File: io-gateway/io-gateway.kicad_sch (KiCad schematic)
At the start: 8 parts, among them J1 1752201, J2 1752201, J3 1752201, J4 Screw_Terminal_01x09, J5 Screw_Terminal_01x09, J6 Screw_Terminal_01x09

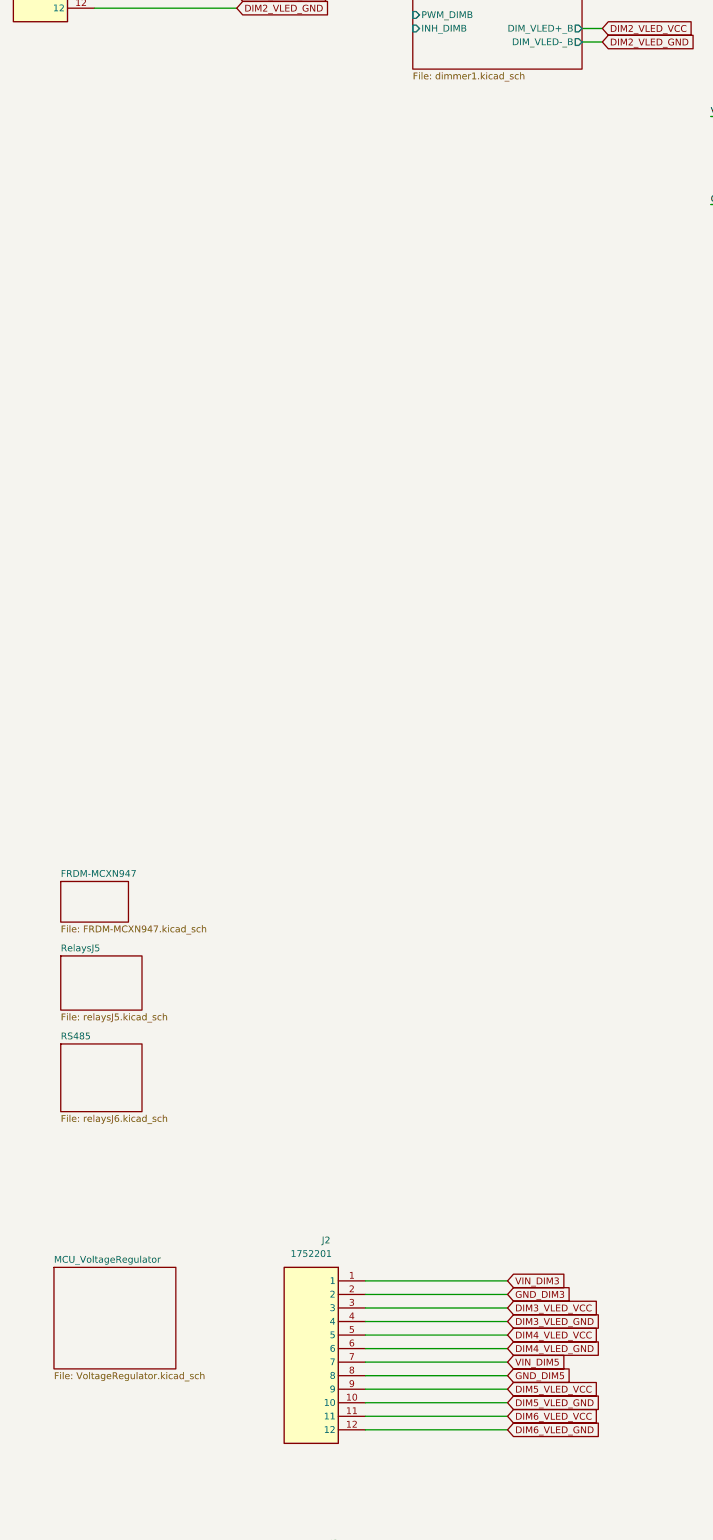
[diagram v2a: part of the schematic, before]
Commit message: reannotate dimmers and relays
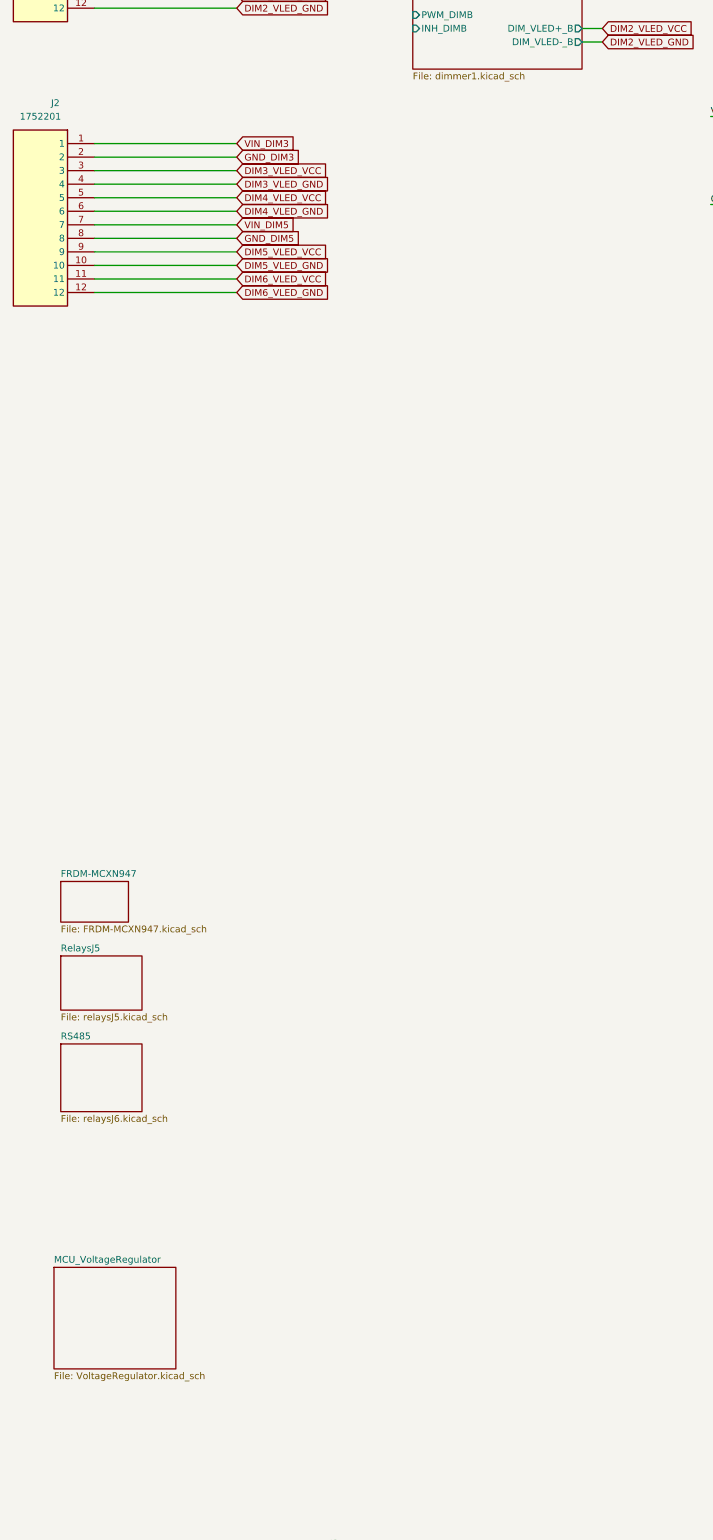
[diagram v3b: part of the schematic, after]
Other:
- moved on the sheet: J2
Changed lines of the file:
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@@
 	(wire
 		(pts
-			(xy 87.63 302.26) (xy 114.3 302.26)
+			(xy 36.83 88.9) (xy 63.5 88.9)
 		)
 		(stroke
@@
 	(wire
 		(pts
-			(xy 87.63 294.64) (xy 114.3 294.64)
+			(xy 36.83 81.28) (xy 63.5 81.28)
 		)
 		(stroke
@@
 	(wire
 		(pts
-			(xy 87.63 322.58) (xy 114.3 322.58)
+			(xy 36.83 109.22) (xy 63.5 109.22)
 		)
 		(stroke
@@
 	(wire
 		(pts
-			(xy 87.63 297.18) (xy 114.3 297.18)
+			(xy 36.83 83.82) (xy 63.5 83.82)
 		)
 		(stroke
@@
 	(wire
 		(pts
-			(xy 87.63 307.34) (xy 114.3 307.34)
+			(xy 36.83 93.98) (xy 63.5 93.98)
 		)
 		(stroke
@@
 	(wire
 		(pts
-			(xy 87.63 312.42) (xy 114.3 312.42)
+			(xy 36.83 99.06) (xy 63.5 99.06)
 		)
 		(stroke
@@
 	(wire
 		(pts
-			(xy 87.63 304.8) (xy 114.3 304.8)
+			(xy 36.83 91.44) (xy 63.5 91.44)
 		)
 		(stroke
@@
 	(wire
 		(pts
-			(xy 87.63 317.5) (xy 114.3 317.5)
+			(xy 36.83 104.14) (xy 63.5 104.14)
 		)
 		(stroke
@@
 	(wire
 		(pts
-			(xy 87.63 299.72) (xy 114.3 299.72)
+			(xy 36.83 86.36) (xy 63.5 86.36)
 		)
 		(stroke
@@
 	(wire
 		(pts
-			(xy 87.63 309.88) (xy 114.3 309.88)
+			(xy 36.83 96.52) (xy 63.5 96.52)
 		)
 		(stroke
@@
 	(wire
 		(pts
-			(xy 87.63 314.96) (xy 114.3 314.96)
-		)
-		(stroke
-			(width 0)
-			(type default)
-		)
-	)
-	(wire
-		(pts
-			(xy 87.63 320.04) (xy 114.3 320.04)
+			(xy 36.83 101.6) (xy 63.5 101.6)
+		)
+		(stroke
+			(width 0)
+			(type default)
+		)
+	)
+	(wire
+		(pts
+			(xy 36.83 106.68) (xy 63.5 106.68)
 		)
 		(stroke
@@
 	(global_label "DIM3_VLED_VCC"
 		(shape input)
-		(at 114.3 299.72 0)
-		(fields_autoplaced yes)
-		(effects
-			(font
-				(size 1.27 1.27)
-			)
-			(justify left)
-		)
-		(property "Intersheetrefs" "${INTERSHEET_REFS}"
-			(at 128.8966 299.72 0)
+		(at 63.5 86.36 0)
+		(fields_autoplaced yes)
+		(effects
+			(font
+				(size 1.27 1.27)
+			)
+			(justify left)
+		)
+		(property "Intersheetrefs" "${INTERSHEET_REFS}"
+			(at 78.0966 86.36 0)
 			(effects
 				(font
@@
 	(global_label "DIM5_VLED_VCC"
 		(shape input)
-		(at 114.3 314.96 0)
-		(fields_autoplaced yes)
-		(effects
-			(font
-				(size 1.27 1.27)
-			)
-			(justify left)
-		)
-		(property "Intersheetrefs" "${INTERSHEET_REFS}"
-			(at 128.8966 314.96 0)
+		(at 63.5 101.6 0)
+		(fields_autoplaced yes)
+		(effects
+			(font
+				(size 1.27 1.27)
+			)
+			(justify left)
+		)
+		(property "Intersheetrefs" "${INTERSHEET_REFS}"
+			(at 78.0966 101.6 0)
 			(effects
 				(font
@@
 	(global_label "DIM6_VLED_VCC"
 		(shape input)
-		(at 114.3 320.04 0)
-		(fields_autoplaced yes)
-		(effects
-			(font
-				(size 1.27 1.27)
-			)
-			(justify left)
-		)
-		(property "Intersheetrefs" "${INTERSHEET_REFS}"
-			(at 128.8966 320.04 0)
+		(at 63.5 106.68 0)
+		(fields_autoplaced yes)
+		(effects
+			(font
+				(size 1.27 1.27)
+			)
+			(justify left)
+		)
+		(property "Intersheetrefs" "${INTERSHEET_REFS}"
+			(at 78.0966 106.68 0)
 			(effects
 				(font
@@
 	(global_label "DIM6_VLED_GND"
 		(shape input)
-		(at 114.3 322.58 0)
-		(fields_autoplaced yes)
-		(effects
-			(font
-				(size 1.27 1.27)
-			)
-			(justify left)
-		)
-		(property "Intersheetrefs" "${INTERSHEET_REFS}"
-			(at 128.8966 322.58 0)
+		(at 63.5 109.22 0)
+		(fields_autoplaced yes)
+		(effects
+			(font
+				(size 1.27 1.27)
+			)
+			(justify left)
+		)
+		(property "Intersheetrefs" "${INTERSHEET_REFS}"
+			(at 78.0966 109.22 0)
 			(effects
 				(font
@@
 	(global_label "GND_DIM5"
 		(shape input)
-		(at 114.3 312.42 0)
-		(fields_autoplaced yes)
-		(effects
-			(font
-				(size 1.27 1.27)
-			)
-			(justify left)
-		)
-		(property "Intersheetrefs" "${INTERSHEET_REFS}"
-			(at 126.659 312.42 0)
+		(at 63.5 99.06 0)
+		(fields_autoplaced yes)
+		(effects
+			(font
+				(size 1.27 1.27)
+			)
+			(justify left)
+		)
+		(property "Intersheetrefs" "${INTERSHEET_REFS}"
+			(at 75.859 99.06 0)
 			(effects
 				(font
@@
 	(global_label "GND_DIM3"
 		(shape input)
-		(at 114.3 297.18 0)
-		(fields_autoplaced yes)
-		(effects
-			(font
-				(size 1.27 1.27)
-			)
-			(justify left)
-		)
-		(property "Intersheetrefs" "${INTERSHEET_REFS}"
-			(at 126.659 297.18 0)
+		(at 63.5 83.82 0)
+		(fields_autoplaced yes)
+		(effects
+			(font
+				(size 1.27 1.27)
+			)
+			(justify left)
+		)
+		(property "Intersheetrefs" "${INTERSHEET_REFS}"
+			(at 75.859 83.82 0)
 			(effects
 				(font
@@
 	(global_label "DIM5_VLED_GND"
 		(shape input)
-		(at 114.3 317.5 0)
-		(fields_autoplaced yes)
-		(effects
-			(font
-				(size 1.27 1.27)
-			)
-			(justify left)
-		)
-		(property "Intersheetrefs" "${INTERSHEET_REFS}"
-			(at 128.8966 317.5 0)
+		(at 63.5 104.14 0)
+		(fields_autoplaced yes)
+		(effects
+			(font
+				(size 1.27 1.27)
+			)
+			(justify left)
+		)
+		(property "Intersheetrefs" "${INTERSHEET_REFS}"
+			(at 78.0966 104.14 0)
 			(effects
 				(font
@@
 	(global_label "VIN_DIM3"
 		(shape input)
-		(at 114.3 294.64 0)
-		(fields_autoplaced yes)
-		(effects
-			(font
-				(size 1.27 1.27)
-			)
-			(justify left)
-		)
-		(property "Intersheetrefs" "${INTERSHEET_REFS}"
-			(at 125.8124 294.64 0)
+		(at 63.5 81.28 0)
+		(fields_autoplaced yes)
+		(effects
+			(font
+				(size 1.27 1.27)
+			)
+			(justify left)
+		)
+		(property "Intersheetrefs" "${INTERSHEET_REFS}"
+			(at 75.0124 81.28 0)
 			(effects
 				(font
@@
 	(global_label "DIM4_VLED_GND"
 		(shape input)
-		(at 114.3 307.34 0)
-		(fields_autoplaced yes)
-		(effects
-			(font
-				(size 1.27 1.27)
-			)
-			(justify left)
-		)
-		(property "Intersheetrefs" "${INTERSHEET_REFS}"
-			(at 128.8966 307.34 0)
+		(at 63.5 93.98 0)
+		(fields_autoplaced yes)
+		(effects
+			(font
+				(size 1.27 1.27)
+			)
+			(justify left)
+		)
+		(property "Intersheetrefs" "${INTERSHEET_REFS}"
+			(at 78.0966 93.98 0)
 			(effects
 				(font
@@
 	(global_label "DIM3_VLED_GND"
 		(shape input)
-		(at 114.3 302.26 0)
-		(fields_autoplaced yes)
-		(effects
-			(font
-				(size 1.27 1.27)
-			)
-			(justify left)
-		)
-		(property "Intersheetrefs" "${INTERSHEET_REFS}"
-			(at 128.8966 302.26 0)
+		(at 63.5 88.9 0)
+		(fields_autoplaced yes)
+		(effects
+			(font
+				(size 1.27 1.27)
+			)
+			(justify left)
+		)
+		(property "Intersheetrefs" "${INTERSHEET_REFS}"
+			(at 78.0966 88.9 0)
 			(effects
 				(font
@@
 	(global_label "VIN_DIM5"
 		(shape input)
-		(at 114.3 309.88 0)
-		(fields_autoplaced yes)
-		(effects
-			(font
-				(size 1.27 1.27)
-			)
-			(justify left)
-		)
-		(property "Intersheetrefs" "${INTERSHEET_REFS}"
-			(at 125.8124 309.88 0)
+		(at 63.5 96.52 0)
+		(fields_autoplaced yes)
+		(effects
+			(font
+				(size 1.27 1.27)
+			)
+			(justify left)
+		)
+		(property "Intersheetrefs" "${INTERSHEET_REFS}"
+			(at 75.0124 96.52 0)
 			(effects
 				(font
@@
 	(global_label "DIM4_VLED_VCC"
 		(shape input)
-		(at 114.3 304.8 0)
-		(fields_autoplaced yes)
-		(effects
-			(font
-				(size 1.27 1.27)
-			)
-			(justify left)
-		)
-		(property "Intersheetrefs" "${INTERSHEET_REFS}"
-			(at 128.8966 304.8 0)
+		(at 63.5 91.44 0)
+		(fields_autoplaced yes)
+		(effects
+			(font
+				(size 1.27 1.27)
+			)
+			(justify left)
+		)
+		(property "Intersheetrefs" "${INTERSHEET_REFS}"
+			(at 78.0966 91.44 0)
 			(effects
 				(font
@@
 	(symbol
 		(lib_id "1752201:1752201")
-		(at 87.63 294.64 0)
+		(at 36.83 81.28 0)
 		(mirror y)
 		(unit 1)
@@
 		(dnp no)
 		(property "Reference" "J2"
-			(at 80.264 287.02 0)
+			(at 29.464 73.66 0)
 			(effects
 				(font
@@
 		)
 		(property "Value" "1752201"
-			(at 77.47 289.56 0)
+			(at 26.67 76.2 0)
 			(effects
 				(font
@@
 		)
 		(property "Footprint" "TerminalBlock_Phoenix:1752201"
-			(at 71.12 389.56 0)
+			(at 20.32 176.2 0)
 			(effects
 				(font
@@
 		)
 		(property "Datasheet" "https://datasheet.datasheetarchive.com/originals/distributors/DKDS-31/613023.pdf"
-			(at 71.12 489.56 0)
+			(at 20.32 276.2 0)
 			(effects
 				(font
@@
 		)
 		(property "Description" "PCB Terminal Block 1752201"
-			(at 87.63 294.64 0)
+			(at 36.83 81.28 0)
 			(effects
 				(font
@@
 		)
 		(property "Height" "12.55"
-			(at 71.12 689.56 0)
+			(at 20.32 476.2 0)
 			(effects
 				(font
@@
 		)
 		(property "Mouser Part Number" "651-1752201"
-			(at 71.12 789.56 0)
+			(at 20.32 576.2 0)
 			(effects
 				(font
@@
 		)
 		(property "Mouser Price/Stock" "https://www.mouser.co.uk/ProductDetail/Phoenix-Contact/1752201?qs=Fz3yxlUjJZGkBSHClOzTtg%3D%3D"
-			(at 71.12 889.56 0)
+			(at 20.32 676.2 0)
 			(effects
 				(font
@@
 		)
 		(property "Manufacturer_Name" "Phoenix Contact"
-			(at 71.12 989.56 0)
+			(at 20.32 776.2 0)
 			(effects
 				(font
@@
 		)
 		(property "Manufacturer_Part_Number" "1752201"
-			(at 71.12 1089.56 0)
-			(effects
-				(font
+			(at 20.32 876.2 0)
+			(effects
+				(font

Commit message: temp
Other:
- added sheet Dimmer2 (dimmer1.kicad_sch)
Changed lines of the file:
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@@
+	)
+	(sheet
+		(at 96.52 77.47)
+		(size 31.75 26.67)
+		(exclude_from_sim no)
+		(in_bom yes)
+		(on_board yes)
+		(dnp no)
+		(fields_autoplaced yes)
+		(stroke
+			(width 0.1524)
+			(type solid)
+		)
+		(fill
+			(color 0 0 0 0.0000)
+		)
+		(property "Sheetname" "Dimmer2"
+			(at 96.52 76.7584 0)
+			(effects
+				(font
+					(size 1.27 1.27)
+				)
+				(justify left bottom)
+			)
+		)
+		(property "Sheetfile" "dimmer1.kicad_sch"
+			(at 96.52 104.7246 0)
+			(effects
+				(font
+					(size 1.27 1.27)
+				)
+				(justify left top)
+			)
+		)
+		(pin "DIM_VLED+_A" output
+			(at 128.27 82.55 0)
+			(effects
+				(font
+					(size 1.27 1.27)
+				)
+				(justify right)
+			)
+		)
+		(pin "DIM_VLED+_B" output
+			(at 128.27 96.52 0)
+			(effects
+				(font
+					(size 1.27 1.27)
+				)
+				(justify right)
+			)
+		)
+		(pin "DIM_VLED-_A" output
+			(at 128.27 85.09 0)
+			(effects
+				(font
+					(size 1.27 1.27)
+				)
+				(justify right)
+			)
+		)
+		(pin "DIM_VLED-_B" output
+			(at 128.27 99.06 0)
+			(effects
+				(font
+					(size 1.27 1.27)
+				)
+				(justify right)
+			)
+		)
+		(pin "GND_DIM" input
+			(at 96.52 82.55 180)
+			(effects
+				(font
+					(size 1.27 1.27)
+				)
+				(justify left)
+			)
+		)
+		(pin "INH_DIMA" input
+			(at 96.52 88.9 180)
+			(effects
+				(font
+					(size 1.27 1.27)
+				)
+				(justify left)
+			)
+		)
+		(pin "INH_DIMB" input
+			(at 96.52 96.52 180)
+			(effects
+				(font
+					(size 1.27 1.27)
+				)
+				(justify left)
+			)
+		)
+		(pin "PWM_DIMA" input
+			(at 96.52 86.36 180)
+			(effects
+				(font
+					(size 1.27 1.27)
+				)
+				(justify left)
+			)
+		)
+		(pin "PWM_DIMB" input
+			(at 96.52 93.98 180)
+			(effects
+				(font
+					(size 1.27 1.27)
+				)
+				(justify left)
+			)
+		)
+		(pin "VIN_DIM" input
+			(at 96.52 80.01 180)
+			(effects
+				(font
+					(size 1.27 1.27)
+				)
+				(justify left)
+			)
+		)
+		(instances
+			(project "io-gateway"
+				(path "/2cb6f94b-272a-4ed7-b08d-c3630bda6156"
+					(page "17")
+				)
+			)
+		)
 	)
 	(sheet

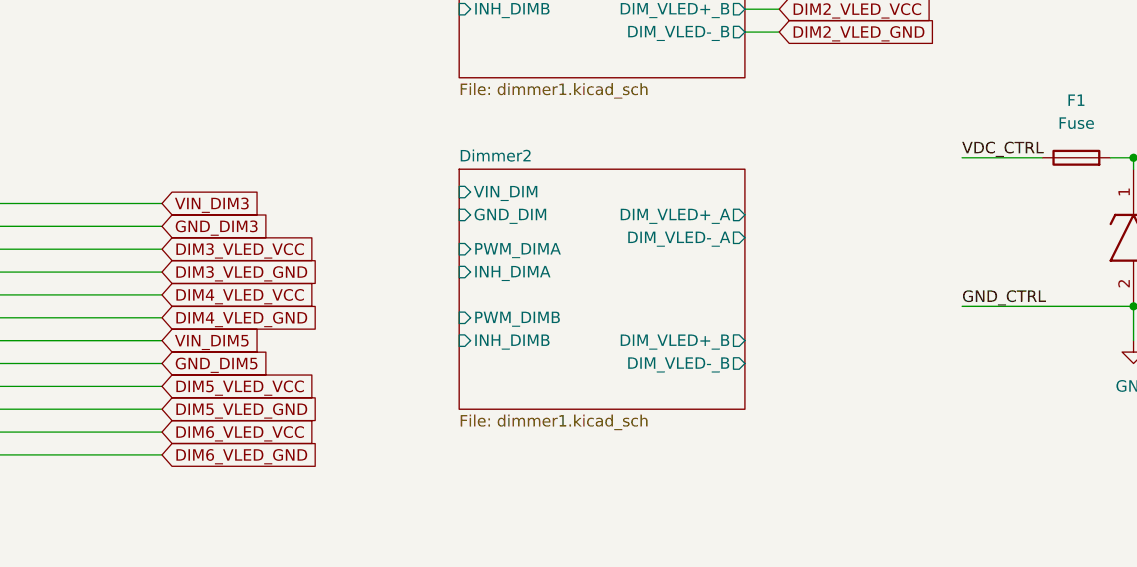
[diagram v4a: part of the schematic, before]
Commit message: duplicate dimmer
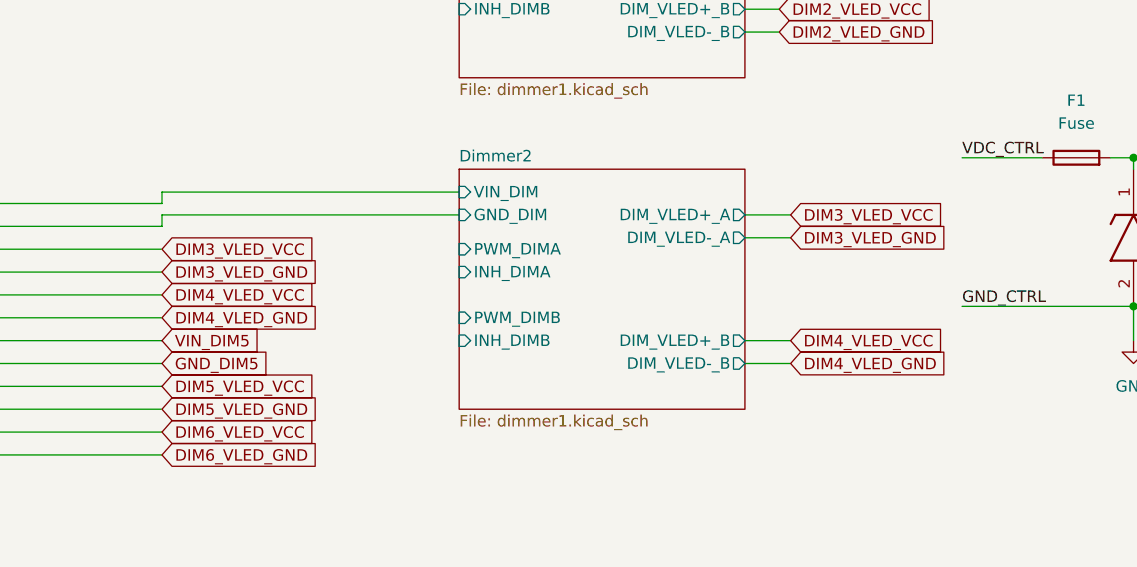
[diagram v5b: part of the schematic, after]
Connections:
- net Dimmer2/GND_DIM: now also J2.2
- net Dimmer2/VIN_DIM: now also J2.1
- net GND_DIM3: no longer J2.2
- net VIN_DIM3: no longer J2.1
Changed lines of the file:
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@@
+	(wire
+		(pts
+			(xy 128.27 99.06) (xy 133.35 99.06)
+		)
+		(stroke
+			(width 0)
+			(type default)
+		)
+	)
 	(wire
 		(pts
@@
 	(wire
 		(pts
+			(xy 128.27 85.09) (xy 133.35 85.09)
+		)
+		(stroke
+			(width 0)
+			(type default)
+		)
+	)
+	(wire
+		(pts
 			(xy 128.27 59.69) (xy 132.08 59.69)
 		)
@@
 	(wire
 		(pts
+			(xy 128.27 82.55) (xy 133.35 82.55)
+		)
+		(stroke
+			(width 0)
+			(type default)
+		)
+	)
+	(wire
+		(pts
 			(xy 254 86.36) (xy 254 78.74)
 		)
@@
 	(wire
 		(pts
+			(xy 96.52 80.01) (xy 63.5 80.01)
+		)
+		(stroke
+			(width 0)
+			(type default)
+		)
+	)
+	(wire
+		(pts
 			(xy 36.83 40.64) (xy 63.5 40.64)
 		)
@@
 	(wire
 		(pts
+			(xy 63.5 80.01) (xy 63.5 81.28)
+		)
+		(stroke
+			(width 0)
+			(type default)
+		)
+	)
+	(wire
+		(pts
 			(xy 280.67 133.35) (xy 280.67 142.24)
 		)
@@
 	(wire
 		(pts
+			(xy 63.5 82.55) (xy 63.5 83.82)
+		)
+		(stroke
+			(width 0)
+			(type default)
+		)
+	)
+	(wire
+		(pts
 			(xy 88.9 377.19) (xy 114.3 377.19)
 		)
@@
 		(pts
 			(xy 128.27 62.23) (xy 132.08 62.23)
+		)
+		(stroke
+			(width 0)
+			(type default)
+		)
+	)
+	(wire
+		(pts
+			(xy 128.27 96.52) (xy 133.35 96.52)
+		)
+		(stroke
+			(width 0)
+			(type default)
+		)
+	)
+	(wire
+		(pts
+			(xy 96.52 82.55) (xy 63.5 82.55)
 		)
 		(stroke
@@
 		)
 	)
+	(global_label "DIM3_VLED_GND"
+		(shape input)
+		(at 133.35 85.09 0)
+		(fields_autoplaced yes)
+		(effects
+			(font
+				(size 1.27 1.27)
+			)
+			(justify left)
+		)
+		(property "Intersheetrefs" "${INTERSHEET_REFS}"
+			(at 147.9466 85.09 0)
+			(effects
+				(font
+					(size 1.27 1.27)
+				)
+				(justify left)
+				(hide yes)
+			)
+		)
+	)
+	(global_label "DIM4_VLED_VCC"
+		(shape input)
+		(at 133.35 96.52 0)
+		(fields_autoplaced yes)
+		(effects
+			(font
+				(size 1.27 1.27)
+			)
+			(justify left)
+		)
+		(property "Intersheetrefs" "${INTERSHEET_REFS}"
+			(at 147.9466 96.52 0)
+			(effects
+				(font
+					(size 1.27 1.27)
+				)
+				(justify left)
+				(hide yes)
+			)
+		)
+	)
 	(global_label "GND_DIM5"
 		(shape input)
@@
 		)
 	)
+	(global_label "DIM4_VLED_GND"
+		(shape input)
+		(at 133.35 99.06 0)
+		(fields_autoplaced yes)
+		(effects
+			(font
+				(size 1.27 1.27)
+			)
+			(justify left)
+		)
+		(property "Intersheetrefs" "${INTERSHEET_REFS}"
+			(at 147.9466 99.06 0)
+			(effects
+				(font
+					(size 1.27 1.27)
+				)
+				(justify left)
+				(hide yes)
+			)
+		)
+	)
 	(global_label "DIM2_VLED_VCC"
 		(shape input)
@@
 		)
 	)
-	(global_label "GND_DIM3"
-		(shape input)
-		(at 63.5 83.82 0)
-		(fields_autoplaced yes)
-		(effects
-			(font
-				(size 1.27 1.27)
-			)
-			(justify left)
-		)
-		(property "Intersheetrefs" "${INTERSHEET_REFS}"
-			(at 75.859 83.82 0)
-			(effects
-				(font
-					(size 1.27 1.27)
-				)
-				(justify left)
-				(hide yes)
-			)
-		)
-	)
 	(global_label "DIM8_VLED_VCC"
 		(shape input)
@@
 		)
 	)
-	(global_label "VIN_DIM3"
-		(shape input)
-		(at 63.5 81.28 0)
-		(fields_autoplaced yes)
-		(effects
-			(font
-				(size 1.27 1.27)
-			)
-			(justify left)
-		)
-		(property "Intersheetrefs" "${INTERSHEET_REFS}"
-			(at 75.0124 81.28 0)
-			(effects
-				(font
-					(size 1.27 1.27)
-				)
-				(justify left)
-				(hide yes)
-			)
-		)
-	)
 	(global_label "VIN_DIM5"
 		(shape input)
@@
 			(effects
 				(font
+					(size 1.27 1.27)
+				)
+				(justify left)
+				(hide yes)
+			)
+		)
+	)
+	(global_label "DIM3_VLED_VCC"
+		(shape input)
+		(at 133.35 82.55 0)
+		(fields_autoplaced yes)
+		(effects
+			(font
+				(size 1.27 1.27)
+			)
+			(justify left)
+		)
+		(property "Intersheetrefs" "${INTERSHEET_REFS}"
+			(at 147.9466 82.55 0)
+			(effects
+				(font

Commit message: Place some Relays
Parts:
- F1: footprint Fuse:Fuseholder_Cylinder-5x20mm_Wuerth_696103101002-SMD_Horizontal_Open -> Fuse:Fuse_0603_1608Metric
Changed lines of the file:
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@@
 			)
 		)
-		(property "Footprint" "Fuse:Fuseholder_Cylinder-5x20mm_Wuerth_696103101002-SMD_Horizontal_Open"
+		(property "Footprint" "Fuse:Fuse_0603_1608Metric"
 			(at 165.1 77.978 90)
 			(effects
